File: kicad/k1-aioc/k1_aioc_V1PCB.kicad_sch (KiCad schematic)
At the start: 56 parts, among them J1 Conn_01x07_Male, J2 12401832E402A, J3 SIP 200, J4 SIP 200, U1 MIC5330-SSYML, U2 STM32F373CBTx(OLD), Y1 8MHz/20pF

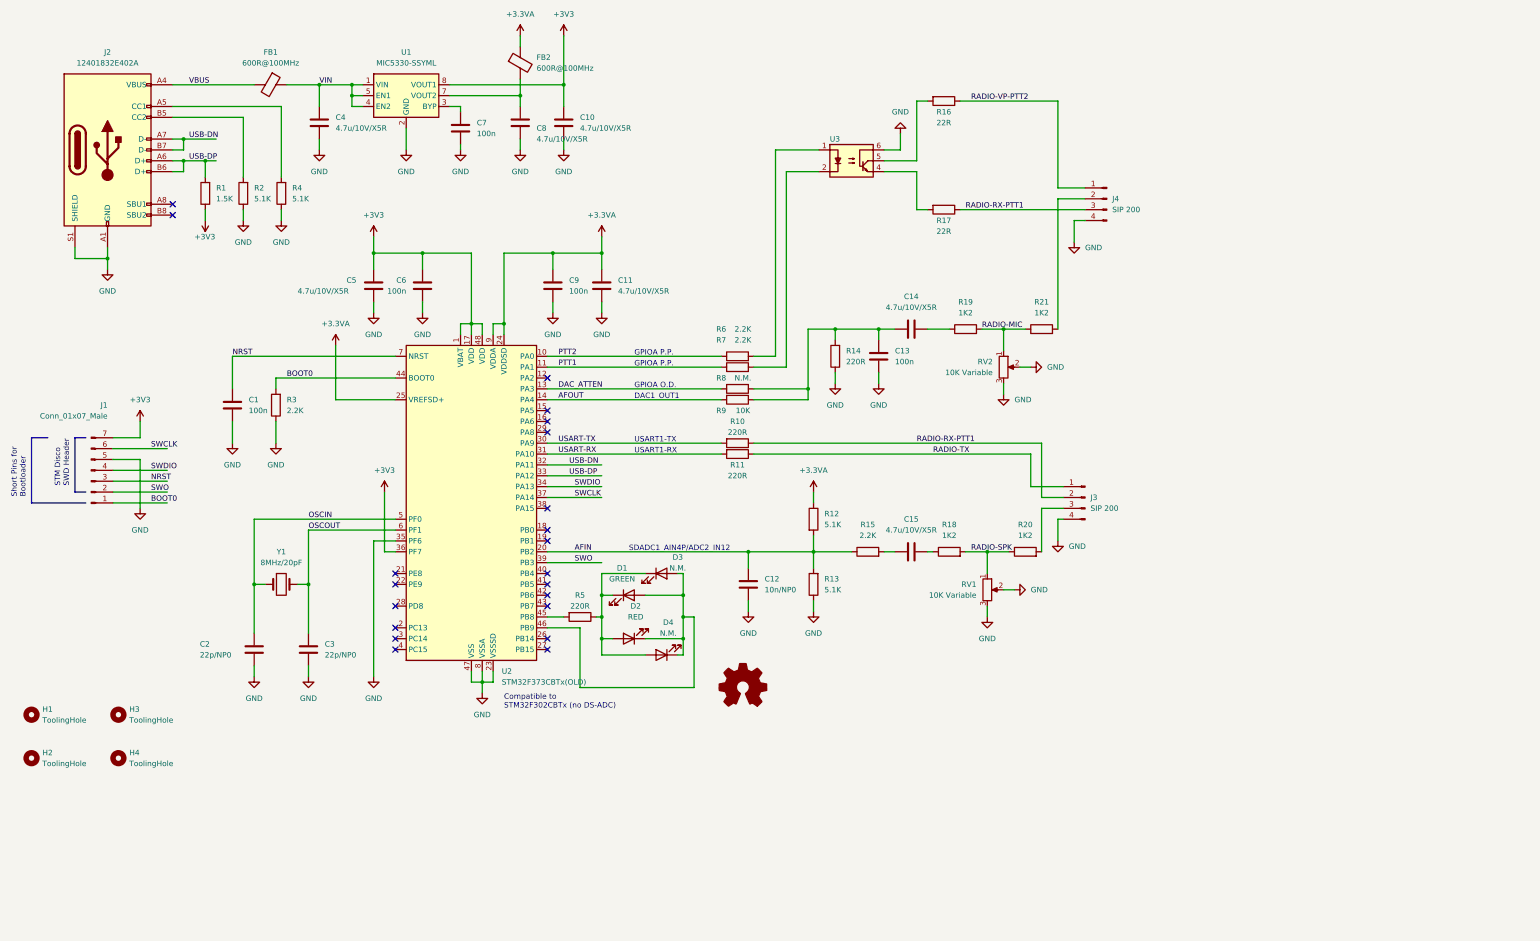
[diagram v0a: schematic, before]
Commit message: updating files and adding usb datasheet
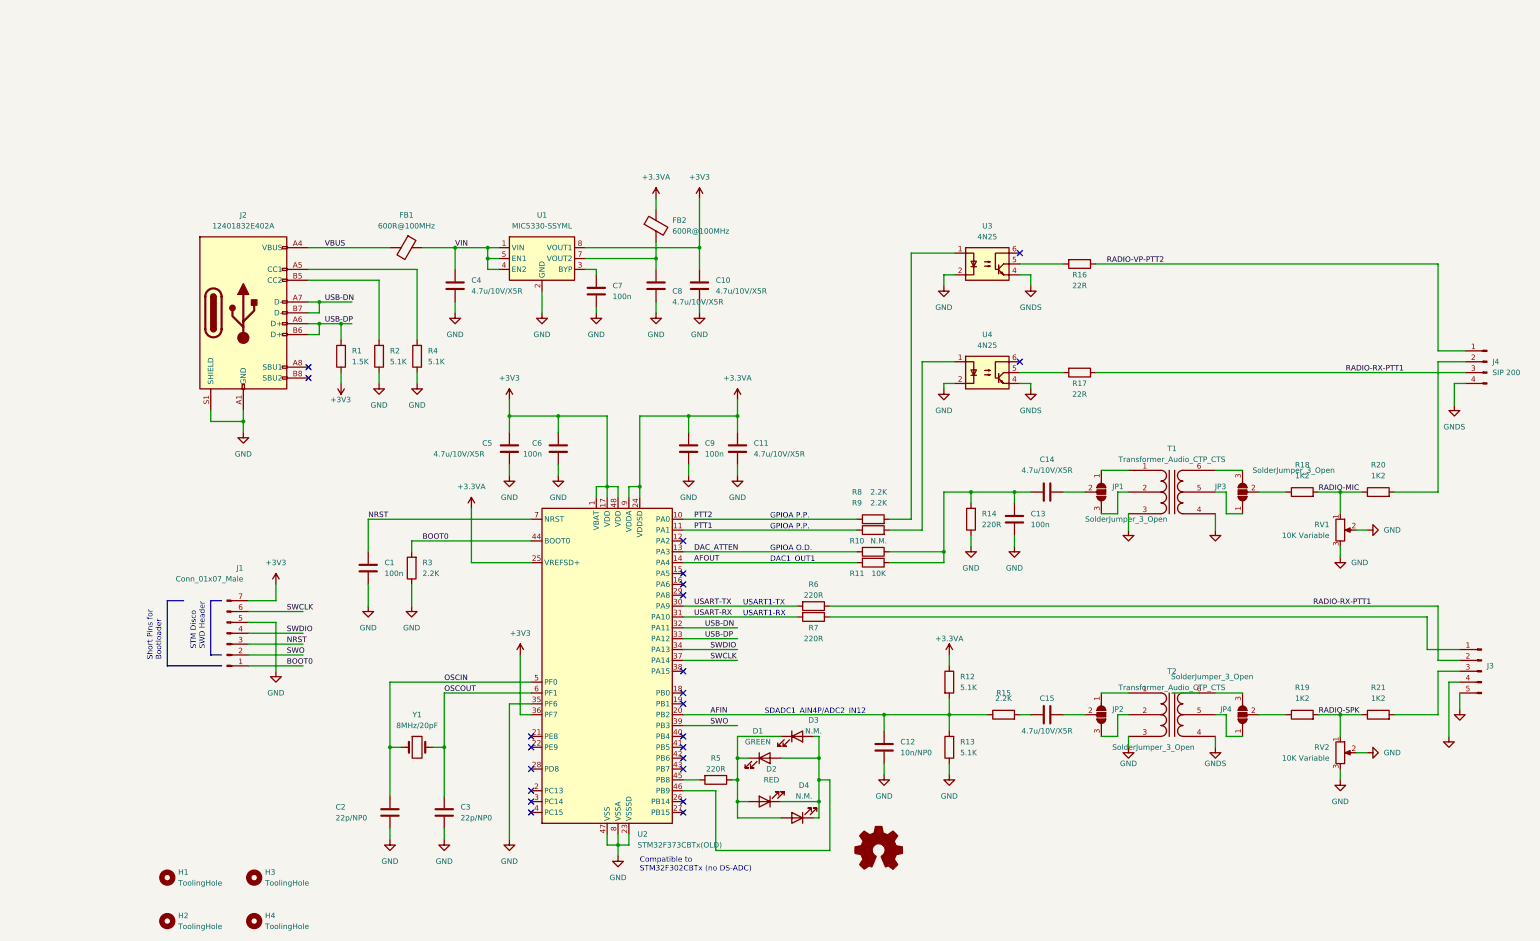
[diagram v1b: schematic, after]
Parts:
- removed J3: SIP 200, TerminalBlock:TerminalBlock_bornier-4_P5.08mm, symbol Connector:Conn_01x04_Male
- removed U3: (no value), Housings_DIP:DIP-6_W7.62mm_SMD, symbol Radio_Digi-rescue:4N25
- added J3: (no value), symbol Connector:Conn_01x05_Male
- added JP1, JP2, JP3, JP4: SolderJumper_3_Open, Jumper:SolderJumper-3_P1.3mm_Open_RoundedPad1.0x1.5mm, symbol Jumper:SolderJumper_3_Open
- added T1, T2: Transformer_Audio_CTP_CTS, AIOC:Transformer_Bourns_SM-LP-5001, symbol Audio_transformer:Transformer_Audio_CTP_CTS
- added U3, U4: 4N25, Package_DIP:DIP-6_W7.62mm, symbol Isolator:4N25
- renumbered R8 to R10, R9 to R11, R19 to R18, R18 to R19, R21 to R20, R20 to R21, R10 to R6, R11 to R7, R6 to R8, R7 to R9, RV2 to RV1, RV1 to RV2
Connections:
- net GND: now also J3.5 (Pin_5), T1.3 (PR2), T2.3 (PR2), U3.2, U4.2; no longer J4.4 (Pin_4)
- net RADIO-RX-PTT1: now also J3.2 (Pin_2)
- net at R18.1: now also JP3.2 (C); no longer C14.2
- net at R16.2: now also U3.5
- net at C15.2: now also JP2.2 (C); no longer R19.1
- net at R8.2: now also U3.1
- net at R9.2: now also U4.1
- net at R17.2: now also U4.5
- net at R21.2: now also J3.3 (Pin_3)
- net RADIO-TX: no longer names the net of R7.1
- net RADIO-TX: now also J3.1 (Pin_1)
- new net: C14.2, JP1.2 (C)
- new net: JP4.2 (C), R19.1
- new net: JP2.1 (A), T2.1 (PR1)
- new net: JP2.3 (B), T2.2 (PM)
- new net: JP3.1 (A), T1.5 (SE)
- new net: JP3.3 (B), T1.6 (S2)
- new net: JP4.1 (A), T2.5 (SE)
- new net: JP4.3 (B), T2.6 (S2)
- new net: JP1.1 (A), T1.1 (PR1)
- new net: JP1.3 (B), T1.2 (PM)
- new net GNDS: J3.4 (Pin_4), J4.4 (Pin_4), T1.4 (S1), T2.4 (S1), U3.4, U4.4
- no-connect marks 21 -> 23
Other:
- title: All-In-One-Cable (AIOC) -> (none)
- moved on the sheet: C1, C10, C11, C12, C13, C14, C15, C2, C3, C4, C5, C6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

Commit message: Updating Kicad files for review
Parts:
- removed J3: (no value), symbol Connector:Conn_01x05_Male
- removed J4: SIP 200, TerminalBlock:TerminalBlock_bornier-4_P5.08mm, symbol Connector:Conn_01x04_Male
- removed R16, R17: 22R, Resistor_SMD:R_0805_2012Metric_Pad1.20x1.40mm_HandSolder, symbol Device:R
- added D5, D6: 1N4001, Diode_SMD:D_0805_2012Metric_Pad1.15x1.40mm_HandSolder, symbol Audio_transformer:D_ALT
- added J3: (no value), symbol Connector:Conn_01x02_Male
- added J4, J6: SIP 200, TerminalBlock:TerminalBlock_bornier-2_P5.08mm, symbol Connector:Conn_01x02_Male
- added J5, J7: SIP 200, TerminalBlock:TerminalBlock_bornier-3_P5.08mm, symbol Connector:Conn_01x03_Male
- added R18, R19: 1K2, Resistor_SMD:R_0805_2012Metric_Pad1.20x1.40mm_HandSolder, symbol Device:R
- H1, H2, H3, H4: footprint AIOC:TOOLING-HOLE -> (none)
- U3, U4: footprint Package_DIP:DIP-6_W7.62mm -> Package_DIP:DIP-6_W8.89mm_SMDSocket_LongPads
- Y1: footprint AIOC:Crystal_SMD_5032-2Pin_5.0x3.2mm -> AIOC:Crystal_8MHz_SMD_11.40mm
- renumbered R18 to R16, R19 to R17
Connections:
- net GND: now also J3.2 (Pin_2), J5.3 (Pin_3); no longer RV1.2, RV1.3, RV2.2, RV2.3
- net GNDS: now also RV1.2, RV1.3, RV2.2, RV2.3, D5.2 (A), D6.2 (A), J5.2 (Pin_2), J7.3 (Pin_3)
- net NRST: now also J3.1 (Pin_1)
- net RADIO-VP-PTT2: now also U3.5, D5.1 (K), J6.1 (Pin_1), R18.1
- net at R20.2: now also J7.1 (Pin_1)
- net at U4.5: now also D6.1 (K), J7.2 (Pin_2), R19.1
- net at R7.1: now also J4.1 (Pin_1)
- net at R21.2: now also J5.1 (Pin_1)
- net RADIO-RX-PTT1: no longer names the net of R6.1
- net RADIO-RX-PTT1: now also J4.2 (Pin_2)
- new net: J6.2 (Pin_2), R18.2, R19.2

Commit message: Updating PCB files
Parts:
- removed JP1, JP2, JP3, JP4: SolderJumper_3_Open, Jumper:SolderJumper-3_P1.3mm_Open_RoundedPad1.0x1.5mm, symbol Jumper:SolderJumper_3_Open
- added JP1, JP2, JP3, JP4: SolderJumper_3_Bridged12, Jumper:SolderJumper-3_P1.3mm_Bridged12_RoundedPad1.0x1.5mm_NumberLabels, symbol Jumper:SolderJumper_3_Bridged12
- C2: value 22p/NP0 -> (none); footprint Capacitor_SMD:C_0805_2012Metric_Pad1.18x1.45mm_HandSolder -> (none)
- H1, H2, H3, H4: footprint (none) -> MountingHole:MountingHole_3.2mm_M3_DIN965_Pad_TopBottom
- J3: value (none) -> conn_01X02; footprint (none) -> Connector_PinHeader_2.54mm:PinHeader_1x02_P2.54mm_Vertical
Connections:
- net at R16.1: now also JP3.2 (C)
- net at C14.2: now also JP1.2 (C)
- net at C15.2: now also JP2.2 (C)
- net at R17.1: now also JP4.2 (C)
- net at T2.1 (PR1): now also JP2.1 (A)
- net at T2.2 (PM): now also JP2.3 (B)
- net at T1.5 (SE): now also JP3.3 (B)
- net at T1.6 (S2): now also JP3.1 (A)
- net at T2.5 (SE): now also JP4.3 (B)
- net at T2.6 (S2): now also JP4.1 (A)
- net at T1.1 (PR1): now also JP1.1 (A)
- net at T1.2 (PM): now also JP1.3 (B)
